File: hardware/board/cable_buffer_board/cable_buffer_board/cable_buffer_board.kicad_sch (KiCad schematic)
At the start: 10 parts, among them J1 Conn_01x01_Socket, J2 Conn_01x06_Female, U2 LTC6269xMS8E

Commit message: draft buffer board
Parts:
- R1: footprint Resistor_SMD:R_0603_1608Metric -> Resistor_SMD:R_0402_1005Metric
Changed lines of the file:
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@@
 			)
 		)
-		(property "Footprint" "Resistor_SMD:R_0603_1608Metric"
+		(property "Footprint" "Resistor_SMD:R_0402_1005Metric"
 			(at 108.077 80.01 90)
 			(effects

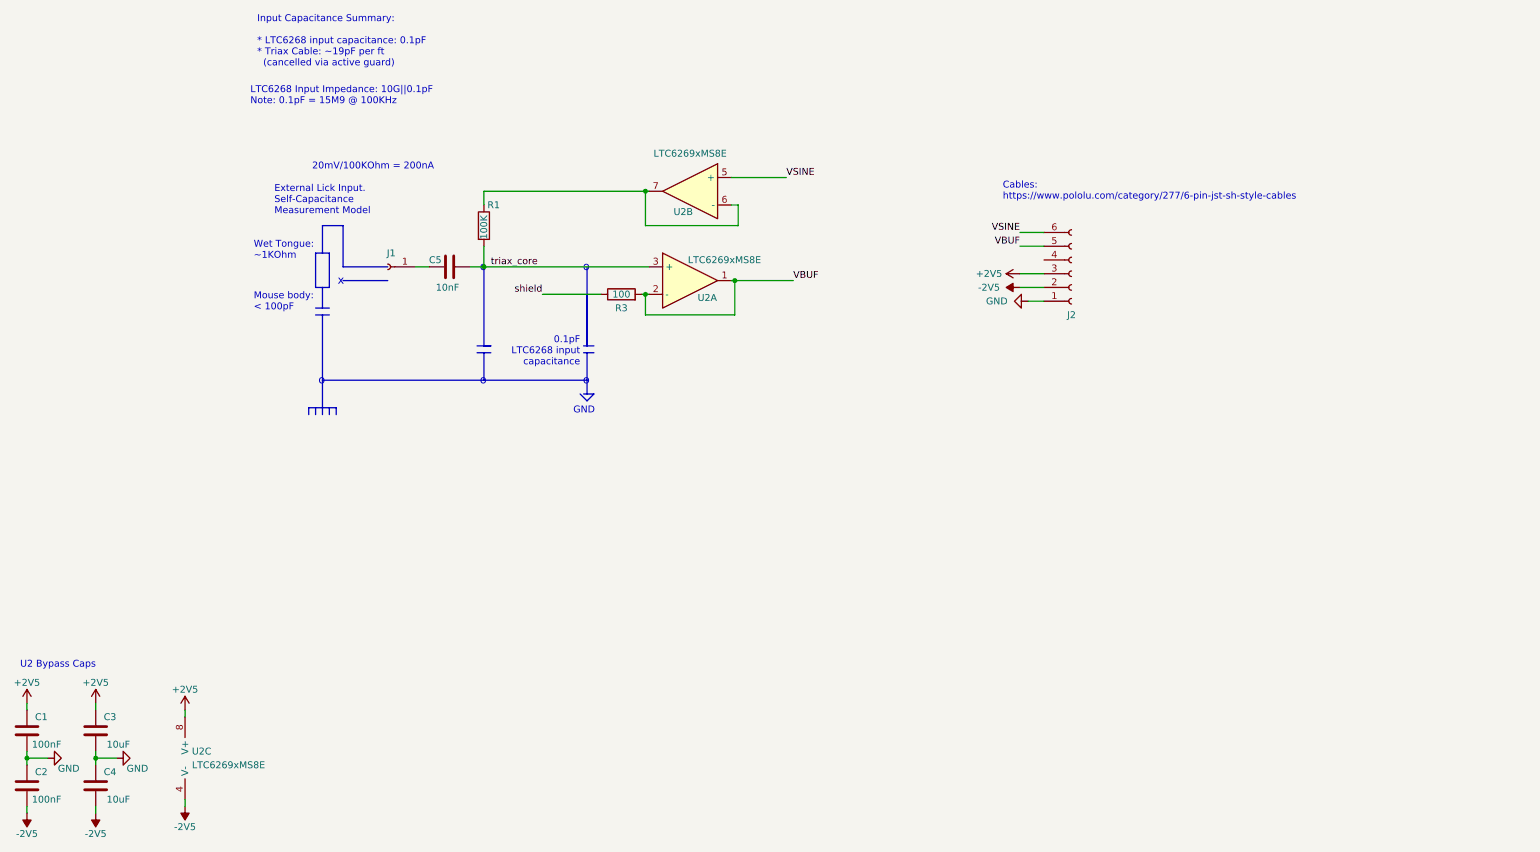
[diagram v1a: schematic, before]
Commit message: split board into two
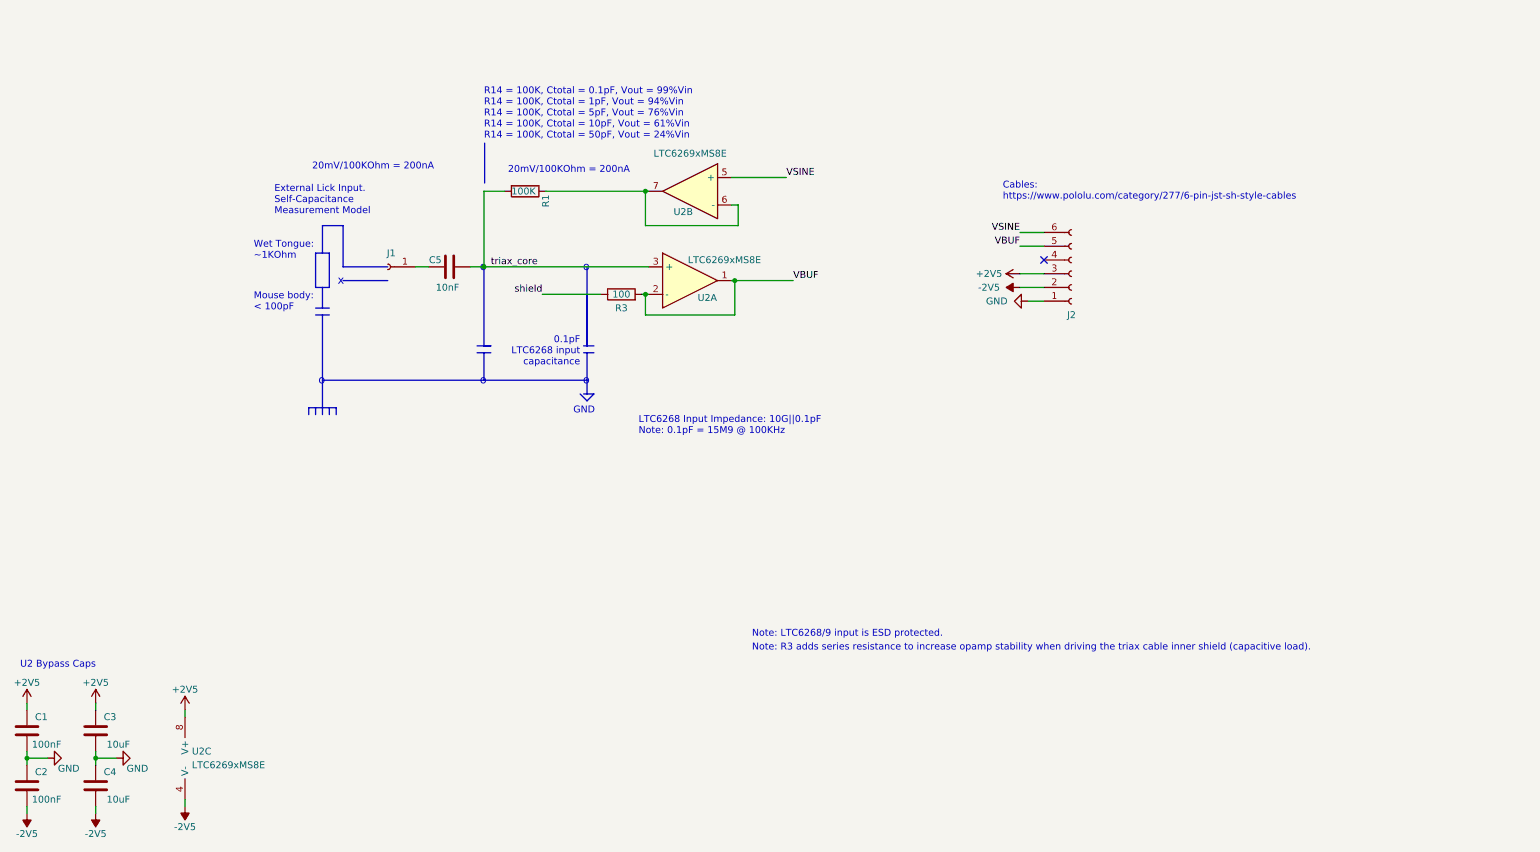
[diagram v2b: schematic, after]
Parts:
- C5: footprint Capacitor_SMD:C_0402_1005Metric -> Capacitor_SMD:C_0402_1005Metric_Pad0.74x0.62mm_HandSolder
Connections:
- no-connect marks 0 -> 1
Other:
- note added: "Note: LTC6268/9 input is ESD protected."
- note added: "Note: R3 adds series resistance to increase opamp stability when driving the triax cable inner shield (capacitive load)."
- note added: "R14 = 100K, Ctotal = 0.1pF, Vout = 99%Vin R14 = 100K, Ctotal = 1pF, Vout = 94%Vin R14 = 100K, Ctotal = 5pF, Vout = 76%Vin R14 = 100K, Ctotal = 10pF, Vout = 61%Vin R14 = 100K, Ctotal = 50pF, Vout = 24%Vin"
- note removed: "Input Capacitance Summary: * LTC6268 input capacitance: 0.1pF * Triax Cable: ~19pF per ft (cancelled via active guard)"
- moved on the sheet: R1
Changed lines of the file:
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@@
 		(color 0 0 0 0)
 	)
+	(no_connect
+		(at 213.36 86.36)
+	)
 	(wire
 		(pts
@@
 	(wire
 		(pts
-			(xy 109.855 73.66) (xy 139.7 73.66)
+			(xy 121.285 73.66) (xy 139.7 73.66)
 		)
 		(stroke
@@
 		)
 	)
-	(wire
-		(pts
-			(xy 109.855 83.82) (xy 109.855 87.63)
-		)
-		(stroke
-			(width 0)
-			(type default)
-		)
-	)
 	(polyline
 		(pts
@@
 		)
 	)
+	(wire
+		(pts
+			(xy 113.665 73.66) (xy 109.855 73.66)
+		)
+		(stroke
+			(width 0)
+			(type default)
+		)
+	)
 	(polyline
 		(pts
@@
 	(polyline
 		(pts
+			(xy 109.982 64.77) (xy 109.982 72.136)
+		)
+		(stroke
+			(width 0)
+			(type default)
+		)
+	)
+	(polyline
+		(pts
 			(xy 78.74 113.665) (xy 78.74 114.935)
 		)
@@
 	(wire
 		(pts
+			(xy 109.855 73.66) (xy 109.855 87.63)
+		)
+		(stroke
+			(width 0)
+			(type default)
+		)
+	)
+	(wire
+		(pts
 			(xy 208.915 81.28) (xy 213.36 81.28)
 		)
@@
 	(wire
 		(pts
-			(xy 109.855 73.66) (xy 109.855 76.2)
-		)
-		(stroke
-			(width 0)
-			(type default)
-		)
-	)
-	(wire
-		(pts
 			(xy 38.1 177.165) (xy 38.1 178.435)
 		)
@@
 	(text "LTC6268 Input Impedance: 10G||0.1pF\nNote: 0.1pF = 15M9 @ 100KHz"
 		(exclude_from_sim no)
-		(at 66.675 57.785 0)
+		(at 138.43 118.745 0)
 		(effects
 			(font
@@
 		)
 	)
-	(text "Input Capacitance Summary:\n\n* LTC6268 input capacitance: 0.1pF\n* Triax Cable: ~19pF per ft \n  (cancelled via active guard)"
-		(exclude_from_sim no)
-		(at 67.945 50.8 0)
+	(text "R14 = 100K, Ctotal = 0.1pF, Vout = 99%Vin\nR14 = 100K, Ctotal = 1pF, Vout = 94%Vin\nR14 = 100K, Ctotal = 5pF, Vout = 76%Vin\nR14 = 100K, Ctotal = 10pF, Vout = 61%Vin\nR14 = 100K, Ctotal = 50pF, Vout = 24%Vin"
+		(exclude_from_sim no)
+		(at 109.855 64.135 0)
 		(effects
 			(font
@@
 			(font
 				(size 1.5 1.5)
+			)
+			(justify left bottom)
+		)
+	)
+	(text "Note: R3 adds series resistance to increase opamp stability when driving the triax cable inner shield (capacitive load)."
+		(exclude_from_sim no)
+		(at 159.385 158.75 0)
+		(effects
+			(font
+				(size 1.27 1.27)
+			)
+			(justify left bottom)
+		)
+	)
+	(text "20mV/100KOhm = 200nA"
+		(exclude_from_sim no)
+		(at 114.3 70.485 0)
+		(effects
+			(font
+				(size 1.27 1.27)
+			)
+			(justify left bottom)
+		)
+	)
+	(text "Note: LTC6268/9 input is ESD protected."
+		(exclude_from_sim no)
+		(at 159.385 156.21 0)
+		(effects
+			(font
+				(size 1.27 1.27)
 			)
 			(justify left bottom)
@@
 	(symbol
 		(lib_id "Device:R")
-		(at 109.855 80.01 0)
+		(at 117.475 73.66 270)
 		(unit 1)
 		(exclude_from_sim no)
@@
 		(dnp no)
 		(property "Reference" "R1"
-			(at 110.49 76.2 0)
+			(at 121.285 74.295 0)
 			(effects
 				(font
@@
 		)
 		(property "Value" "100K"
-			(at 109.855 82.55 90)
+			(at 114.935 73.66 90)
 			(effects
 				(font
@@
 		)
 		(property "Footprint" "Resistor_SMD:R_0402_1005Metric"
-			(at 108.077 80.01 90)
+			(at 117.475 71.882 90)
 			(effects
 				(font
@@
 		)
 		(property "Datasheet" "n/a"
-			(at 109.855 80.01 0)
+			(at 117.475 73.66 0)
 			(effects
 				(font
@@
 		)
 		(property "Description" ""
-			(at 109.855 80.01 0)
+			(at 117.475 73.66 0)
 			(effects
 				(font
@@
 		)
 		(property "Link" ""
-			(at 109.855 80.01 0)
+			(at 117.475 73.66 0)
 			(effects
 				(font
@@
 		)
 		(property "Manufacturer" "Yageo"
-			(at 109.855 80.01 0)
+			(at 117.475 73.66 0)
 			(effects
 				(font
@@
 		)
 		(property "Manufacturer Number" ""
-			(at 109.855 80.01 0)
+			(at 117.475 73.66 0)
 			(effects
 				(font
@@
 		)
 		(property "Tolerance" "1%"
-			(at 109.855 80.01 0)
+			(at 117.475 73.66 0)
 			(effects
 				(font
@@
 		)
 		(property "Notes" ""
-			(at 109.855 80.01 0)
+			(at 117.475 73.66 0)
 			(effects
 				(font
@@
 			)
 		)
-		(property "Footprint" "Capacitor_SMD:C_0402_1005Metric"
+		(property "Footprint" "Capacitor_SMD:C_0402_1005Metric_Pad0.74x0.62mm_HandSolder"
 			(at 99.695 88.5952 0)
 			(effects

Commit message: update buffer board soldermask cutout
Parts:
- U2: Link https://www.digikey.com/en/products/detail/analog-devices-inc/LTC6269HDD-10-PBF/5253541 -> https://www.digikey.com/en/products/detail/analog-devices-inc/LTC6269IMS8E-PBF/5030347; Manufacturer (none) -> Analog Devices Inc.; Manufacturer Number (none) -> LTC6269IMS8E#PBF
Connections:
- net triax_core: no longer names the net of C5.1, R1.2, U2.3 (+)
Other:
- note removed: "x"
- title: (none) -> Lickety Split Capacitive Lick Detector: Buffer Board
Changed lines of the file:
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@@
 	(generator_version "8.0")
 	(paper "A4")
+	(title_block
+		(title "Lickety Split Capacitive Lick Detector: Buffer Board")
+		(rev "1.0.0")
+	)
 	(junction
 		(at 139.7 73.66)
@@
 		)
 	)
-	(polyline
-		(pts
-			(xy 83.82 90.17) (xy 92.075 90.17)
-		)
-		(stroke
-			(width 0)
-			(type default)
-		)
-	)
 	(wire
 		(pts
@@
 			)
 			(justify left)
-		)
-	)
-	(text "x"
-		(exclude_from_sim no)
-		(at 82.804 91.186 0)
-		(effects
-			(font
-				(size 1.5 1.5)
-			)
-			(justify left bottom)
 		)
 	)
@@
 		)
 	)
-	(label "triax_core"
-		(at 111.125 87.63 0)
-		(fields_autoplaced yes)
-		(effects
-			(font
-				(size 1.27 1.27)
-			)
-			(justify left bottom)
-		)
-	)
 	(label "shield"
 		(at 120.65 92.71 180)
@@
 			)
 		)
-		(property "Link" "https://www.digikey.com/en/products/detail/analog-devices-inc/LTC6269HDD-10-PBF/5253541"
+		(property "Link" "https://www.digikey.com/en/products/detail/analog-devices-inc/LTC6269IMS8E-PBF/5030347"
+			(at 147.955 73.66 0)
+			(effects
+				(font
+					(size 1.27 1.27)
+				)
+				(hide yes)
+			)
+		)
+		(property "Manufacturer" "Analog Devices Inc."
+			(at 147.955 73.66 0)
+			(effects
+				(font
+					(size 1.27 1.27)
+				)
+				(hide yes)
+			)
+		)
+		(property "Manufacturer Number" "LTC6269IMS8E#PBF"
 			(at 147.955 73.66 0)
 			(effects
@@
 			)
 		)
-		(property "Link" "https://www.digikey.com/en/products/detail/analog-devices-inc/LTC6269HDD-10-PBF/5253541"
+		(property "Link" "https://www.digikey.com/en/products/detail/analog-devices-inc/LTC6269IMS8E-PBF/5030347"
+			(at 57.15 178.435 0)
+			(effects
+				(font
+					(size 1.27 1.27)
+				)
+				(hide yes)
+			)
+		)
+		(property "Manufacturer" "Analog Devices Inc."
+			(at 57.15 178.435 0)
+			(effects
+				(font
+					(size 1.27 1.27)
+				)
+				(hide yes)
+			)
+		)
+		(property "Manufacturer Number" "LTC6269IMS8E#PBF"
 			(at 57.15 178.435 0)
 			(effects
@@
 			)
 		)
-		(property "Link" "https://www.digikey.com/en/products/detail/analog-devices-inc/LTC6269HDD-10-PBF/5253541"
+		(property "Link" "https://www.digikey.com/en/products/detail/analog-devices-inc/LTC6269IMS8E-PBF/5030347"
 			(at 147.955 90.17 0)
 			(effects
+				(font
+					(size 1.27 1.27)
+				)
+				(hide yes)
+			)
+		)
+		(property "Manufacturer" "Analog Devices Inc."
+			(at 147.955 90.17 0)
+			(effects
+				(font
+					(size 1.27 1.27)
+				)
+				(hide yes)
+			)
+		)
+		(property "Manufacturer Number" "LTC6269IMS8E#PBF"
+			(at 147.955 90.17 0)
+			(effects

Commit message: add split pcba design
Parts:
- J1: now not fitted
- J2: Link https://www.newark.com/jst-japan-solderless-terminals/sm06b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 -> https://www.digikey.com/en/products/detail/jst-sales-americ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; Manufacturer (none) -> JST Sales America Inc.; Manufacturer Number (none) -> SM06B-SRSS-TB
- R1: Link (none) -> https://www.digikey.com/en/products/detail/yageo/RC0402FR-0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; Manufacturer Number (none) -> RC0402FR-07100KL
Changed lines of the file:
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@@
 			)
 		)
-		(property "Datasheet" "n/a"
+		(property "Datasheet" "https://www.yageo.com/upload/media/product/app/datasheet/rchip/pyu-rt_1-to-0.01_rohs_l.pdf"
 			(at 135.255 92.71 0)
 			(effects
@@
 			)
 		)
-		(property "Datasheet" "n/a"
+		(property "Datasheet" "https://www.yageo.com/upload/media/product/products/datasheet/rchip/PYu-RC_Group_51_RoHS_L_12.pdf"
 			(at 117.475 73.66 0)
 			(effects
@@
 			)
 		)
-		(property "Link" ""
+		(property "Link" "https://www.digikey.com/en/products/detail/yageo/RC0402FR-07100KL/726526"
 			(at 117.475 73.66 0)
 			(effects
@@
 			)
 		)
-		(property "Manufacturer Number" ""
+		(property "Manufacturer Number" "RC0402FR-07100KL"
 			(at 117.475 73.66 0)
 			(effects
@@
 		(in_bom yes)
 		(on_board yes)
-		(dnp no)
+		(dnp yes)
 		(fields_autoplaced yes)
 		(property "Reference" "J1"
@@
 			)
 		)
-		(property "Datasheet" "~"
+		(property "Datasheet" "n/a"
 			(at 92.075 87.63 0)
 			(effects
@@
 			)
 		)
-		(property "Datasheet" "https://www.farnell.com/datasheets/2082363.pdf"
+		(property "Datasheet" "https://www.jst-mfg.com/product/pdf/eng/eSH.pdf"
 			(at 218.44 88.9 0)
 			(effects
@@
 			)
 		)
-		(property "Link" "https://www.newark.com/jst-japan-solderless-terminals/sm06b-srss-tb-lf-sn/connector-header-6pos-1row-1mm/dp/33P8182?ost=sm06b-srss-tb%28lf%29%28sn%29"
+		(property "Link" "https://www.digikey.com/en/products/detail/jst-sales-america-inc/SM06B-SRSS-TB/926712"
 			(at 218.44 88.9 0)
 			(effects
@@
 			(at 218.44 88.9 0)
 			(effects
+				(font
+					(size 1.27 1.27)
+				)
+				(hide yes)
+			)
+		)
+		(property "Manufacturer" "JST Sales America Inc."
+			(at 218.44 88.9 0)
+			(effects
+				(font
+					(size 1.27 1.27)
+				)
+				(hide yes)
+			)
+		)
+		(property "Manufacturer Number" "SM06B-SRSS-TB"
+			(at 218.44 88.9 0)
+			(effects
